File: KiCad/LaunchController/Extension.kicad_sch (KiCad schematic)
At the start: 3 parts, among them J17 CONN_STATUS_PANEL, J22 CONN_PANEL_BAORD_2, J23 CONN_PANEL_BAORD_1

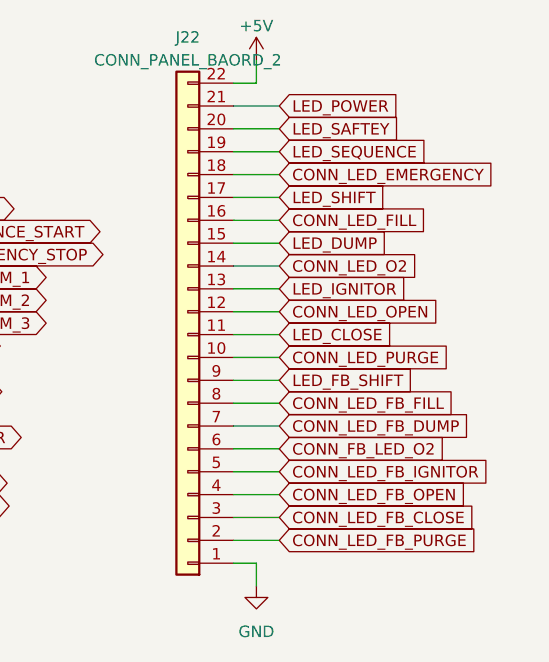
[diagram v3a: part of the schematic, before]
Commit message: シュミットトリガー無しで部品を配置
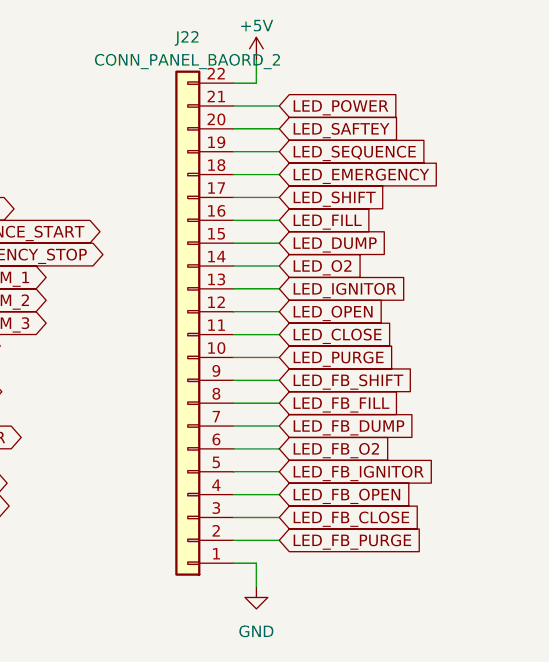
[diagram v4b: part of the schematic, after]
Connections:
- net CONN_FB_LED_O2 renamed LED_FB_O2
- net CONN_LED_EMERGENCY renamed LED_EMERGENCY
- net CONN_LED_FB_CLOSE renamed LED_FB_CLOSE
- net CONN_LED_FB_DUMP renamed LED_FB_DUMP
- net CONN_LED_FB_FILL renamed LED_FB_FILL
- net CONN_LED_FB_IGNITOR renamed LED_FB_IGNITOR
- net CONN_LED_FB_OPEN renamed LED_FB_OPEN
- net CONN_LED_FB_PURGE renamed LED_FB_PURGE
- net CONN_LED_FILL renamed LED_FILL
- net CONN_LED_O2 renamed LED_O2
- net CONN_LED_OPEN renamed LED_OPEN
- net CONN_LED_PURGE renamed LED_PURGE
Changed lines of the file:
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@@
     (stroke (width 0) (type default))
   )
-  (global_label "CONN_LED_FB_CLOSE" (shape input) (at 130.81 81.28 0) (fields_autoplaced)
-    (effects (font (size 1.27 1.27)) (justify left))
-    (property "Intersheetrefs" "${INTERSHEET_REFS}" (at 153.6729 81.28 0)
+  (global_label "LED_FB_CLOSE" (shape input) (at 130.81 81.28 0) (fields_autoplaced)
+    (effects (font (size 1.27 1.27)) (justify left))
+    (property "Intersheetrefs" "${INTERSHEET_REFS}" (at 147.4438 81.28 0)
       (effects (font (size 1.27 1.27)) (justify left) hide)
     )
@@
     )
   )
-  (global_label "CONN_LED_O2" (shape input) (at 130.81 53.34 0) (fields_autoplaced)
-    (effects (font (size 1.27 1.27)) (justify left))
-    (property "Intersheetrefs" "${INTERSHEET_REFS}" (at 146.8996 53.34 0)
-      (effects (font (size 1.27 1.27)) (justify left) hide)
-    )
-  )
-  (global_label "CONN_LED_EMERGENCY" (shape input) (at 130.81 43.18 0) (fields_autoplaced)
-    (effects (font (size 1.27 1.27)) (justify left))
-    (property "Intersheetrefs" "${INTERSHEET_REFS}" (at 155.4871 43.18 0)
-      (effects (font (size 1.27 1.27)) (justify left) hide)
-    )
-  )
-  (global_label "CONN_LED_FB_IGNITOR" (shape input) (at 130.81 76.2 0) (fields_autoplaced)
-    (effects (font (size 1.27 1.27)) (justify left))
-    (property "Intersheetrefs" "${INTERSHEET_REFS}" (at 155.064 76.2 0)
+  (global_label "LED_O2" (shape input) (at 130.81 53.34 0) (fields_autoplaced)
+    (effects (font (size 1.27 1.27)) (justify left))
+    (property "Intersheetrefs" "${INTERSHEET_REFS}" (at 140.6705 53.34 0)
+      (effects (font (size 1.27 1.27)) (justify left) hide)
+    )
+  )
+  (global_label "LED_EMERGENCY" (shape input) (at 130.81 43.18 0) (fields_autoplaced)
+    (effects (font (size 1.27 1.27)) (justify left))
+    (property "Intersheetrefs" "${INTERSHEET_REFS}" (at 149.258 43.18 0)
+      (effects (font (size 1.27 1.27)) (justify left) hide)
+    )
+  )
+  (global_label "LED_FB_IGNITOR" (shape input) (at 130.81 76.2 0) (fields_autoplaced)
+    (effects (font (size 1.27 1.27)) (justify left))
+    (property "Intersheetrefs" "${INTERSHEET_REFS}" (at 148.8349 76.2 0)
       (effects (font (size 1.27 1.27)) (justify left) hide)
     )
@@
     )
   )
-  (global_label "CONN_LED_FB_OPEN" (shape input) (at 130.81 78.74 0) (fields_autoplaced)
-    (effects (font (size 1.27 1.27)) (justify left))
-    (property "Intersheetrefs" "${INTERSHEET_REFS}" (at 152.7658 78.74 0)
-      (effects (font (size 1.27 1.27)) (justify left) hide)
-    )
-  )
-  (global_label "CONN_LED_FB_FILL" (shape input) (at 130.81 68.58 0) (fields_autoplaced)
-    (effects (font (size 1.27 1.27)) (justify left))
-    (property "Intersheetrefs" "${INTERSHEET_REFS}" (at 151.4354 68.58 0)
-      (effects (font (size 1.27 1.27)) (justify left) hide)
-    )
-  )
-  (global_label "CONN_LED_FILL" (shape input) (at 130.81 48.26 0) (fields_autoplaced)
-    (effects (font (size 1.27 1.27)) (justify left))
-    (property "Intersheetrefs" "${INTERSHEET_REFS}" (at 148.1092 48.26 0)
+  (global_label "LED_FB_OPEN" (shape input) (at 130.81 78.74 0) (fields_autoplaced)
+    (effects (font (size 1.27 1.27)) (justify left))
+    (property "Intersheetrefs" "${INTERSHEET_REFS}" (at 146.5367 78.74 0)
+      (effects (font (size 1.27 1.27)) (justify left) hide)
+    )
+  )
+  (global_label "LED_FB_FILL" (shape input) (at 130.81 68.58 0) (fields_autoplaced)
+    (effects (font (size 1.27 1.27)) (justify left))
+    (property "Intersheetrefs" "${INTERSHEET_REFS}" (at 145.2063 68.58 0)
+      (effects (font (size 1.27 1.27)) (justify left) hide)
+    )
+  )
+  (global_label "LED_FILL" (shape input) (at 130.81 48.26 0) (fields_autoplaced)
+    (effects (font (size 1.27 1.27)) (justify left))
+    (property "Intersheetrefs" "${INTERSHEET_REFS}" (at 141.8801 48.26 0)
       (effects (font (size 1.27 1.27)) (justify left) hide)
     )
@@
     )
   )
-  (global_label "CONN_LED_FB_PURGE" (shape input) (at 130.81 83.82 0) (fields_autoplaced)
-    (effects (font (size 1.27 1.27)) (justify left))
-    (property "Intersheetrefs" "${INTERSHEET_REFS}" (at 153.9753 83.82 0)
+  (global_label "LED_FB_PURGE" (shape input) (at 130.81 83.82 0) (fields_autoplaced)
+    (effects (font (size 1.27 1.27)) (justify left))
+    (property "Intersheetrefs" "${INTERSHEET_REFS}" (at 147.7462 83.82 0)
       (effects (font (size 1.27 1.27)) (justify left) hide)
     )
@@
     )
   )
-  (global_label "CONN_LED_OPEN" (shape input) (at 130.81 58.42 0) (fields_autoplaced)
-    (effects (font (size 1.27 1.27)) (justify left))
-    (property "Intersheetrefs" "${INTERSHEET_REFS}" (at 149.4396 58.42 0)
-      (effects (font (size 1.27 1.27)) (justify left) hide)
-    )
-  )
-  (global_label "CONN_LED_FB_DUMP" (shape input) (at 130.81 71.12 0) (fields_autoplaced)
-    (effects (font (size 1.27 1.27)) (justify left))
-    (property "Intersheetrefs" "${INTERSHEET_REFS}" (at 153.0077 71.12 0)
-      (effects (font (size 1.27 1.27)) (justify left) hide)
-    )
-  )
-  (global_label "CONN_FB_LED_O2" (shape input) (at 130.81 73.66 0) (fields_autoplaced)
-    (effects (font (size 1.27 1.27)) (justify left))
-    (property "Intersheetrefs" "${INTERSHEET_REFS}" (at 150.2258 73.66 0)
+  (global_label "LED_OPEN" (shape input) (at 130.81 58.42 0) (fields_autoplaced)
+    (effects (font (size 1.27 1.27)) (justify left))
+    (property "Intersheetrefs" "${INTERSHEET_REFS}" (at 143.2105 58.42 0)
+      (effects (font (size 1.27 1.27)) (justify left) hide)
+    )
+  )
+  (global_label "LED_FB_DUMP" (shape input) (at 130.81 71.12 0) (fields_autoplaced)
+    (effects (font (size 1.27 1.27)) (justify left))
+    (property "Intersheetrefs" "${INTERSHEET_REFS}" (at 146.7786 71.12 0)
+      (effects (font (size 1.27 1.27)) (justify left) hide)
+    )
+  )
+  (global_label "LED_FB_O2" (shape input) (at 130.81 73.66 0) (fields_autoplaced)
+    (effects (font (size 1.27 1.27)) (justify left))
+    (property "Intersheetrefs" "${INTERSHEET_REFS}" (at 143.9967 73.66 0)
       (effects (font (size 1.27 1.27)) (justify left) hide)
     )
@@
     )
   )
-  (global_label "CONN_LED_PURGE" (shape input) (at 130.81 63.5 0) (fields_autoplaced)
-    (effects (font (size 1.27 1.27)) (justify left))
-    (property "Intersheetrefs" "${INTERSHEET_REFS}" (at 150.6491 63.5 0)
-      (effects (font (size 1.27 1.27)) (justify left) hide)
-    )
+  (global_label "LED_PURGE" (shape input) (at 130.81 63.5 0) (fields_autoplaced)
+    (effects (font (size 1.27 1.27)) (justify left))
+    (property "Intersheetrefs" "${INTERSHEET_REFS}" (at 144.42 63.5 0)
+      (effects (font (size 1.27 1.27)) (justify left) hide)
+    )

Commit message: リセット
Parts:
- renumbered J17 to J7, J22 to J8, J23 to J9
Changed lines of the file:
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@@
   (symbol (lib_id "Connector_Generic:Conn_01x22") (at 120.65 60.96 180) (unit 1)
     (in_bom yes) (on_board yes) (dnp no) (fields_autoplaced)
-    (property "Reference" "J22" (at 120.65 27.94 0)
+    (property "Reference" "J8" (at 120.65 27.94 0)
       (effects (font (size 1.27 1.27)))
     )
@@
       (project "LaunchController"
         (path "/628d040b-43bf-4733-804f-091644a90124/7294b7f8-79a7-4ea3-8687-92a673d94882"
-          (reference "J22") (unit 1)
+          (reference "J8") (unit 1)
         )
       )
@@
   (symbol (lib_id "Connector_Generic:Conn_01x18") (at 78.74 62.23 180) (unit 1)
     (in_bom yes) (on_board yes) (dnp no) (fields_autoplaced)
-    (property "Reference" "J23" (at 78.74 34.29 0)
+    (property "Reference" "J9" (at 78.74 34.29 0)
       (effects (font (size 1.27 1.27)))
     )
@@
       (project "LaunchController"
         (path "/628d040b-43bf-4733-804f-091644a90124/7294b7f8-79a7-4ea3-8687-92a673d94882"
-          (reference "J23") (unit 1)
+          (reference "J9") (unit 1)
         )
       )
@@
         )
         (path "/628d040b-43bf-4733-804f-091644a90124/7294b7f8-79a7-4ea3-8687-92a673d94882"
-          (reference "#PWR080") (unit 1)
+          (reference "#PWR049") (unit 1)
         )
       )
@@
         )
         (path "/628d040b-43bf-4733-804f-091644a90124/7294b7f8-79a7-4ea3-8687-92a673d94882"
-          (reference "#PWR083") (unit 1)
+          (reference "#PWR048") (unit 1)
         )
       )
@@
   (symbol (lib_id "Connector_Generic:Conn_01x14") (at 27.94 60.96 180) (unit 1)
     (in_bom yes) (on_board yes) (dnp no) (fields_autoplaced)
-    (property "Reference" "J17" (at 27.94 38.1 0)
+    (property "Reference" "J7" (at 27.94 38.1 0)
       (effects (font (size 1.27 1.27)))
     )
@@
       (project "LaunchController"
         (path "/628d040b-43bf-4733-804f-091644a90124/7294b7f8-79a7-4ea3-8687-92a673d94882"
-          (reference "J17") (unit 1)
+          (reference "J7") (unit 1)
         )
       )
@@
   (symbol (lib_id "power:GND") (at 35.56 78.74 0) (unit 1)
     (in_bom yes) (on_board yes) (dnp no) (fields_autoplaced)
-    (property "Reference" "#PWR067" (at 35.56 85.09 0)
+    (property "Reference" "#PWR051" (at 35.56 85.09 0)
       (effects (font (size 1.27 1.27)) hide)
     )
@@
       (project "LaunchController"
         (path "/628d040b-43bf-4733-804f-091644a90124/7294b7f8-79a7-4ea3-8687-92a673d94882"
-          (reference "#PWR067") (unit 1)
+          (reference "#PWR051") (unit 1)
         )
       )
@@
   (symbol (lib_id "power:GND") (at 86.36 85.09 0) (unit 1)
     (in_bom yes) (on_board yes) (dnp no) (fields_autoplaced)
-    (property "Reference" "#PWR082" (at 86.36 91.44 0)
+    (property "Reference" "#PWR052" (at 86.36 91.44 0)
       (effects (font (size 1.27 1.27)) hide)
     )
@@
       (project "LaunchController"
         (path "/628d040b-43bf-4733-804f-091644a90124/7294b7f8-79a7-4ea3-8687-92a673d94882"
-          (reference "#PWR082") (unit 1)
+          (reference "#PWR052") (unit 1)
         )
       )
@@
         )
         (path "/628d040b-43bf-4733-804f-091644a90124/7294b7f8-79a7-4ea3-8687-92a673d94882"
-          (reference "#PWR079") (unit 1)
+          (reference "#PWR050") (unit 1)
         )
       )
@@
   (symbol (lib_id "power:GND") (at 128.27 88.9 0) (unit 1)
     (in_bom yes) (on_board yes) (dnp no) (fields_autoplaced)
-    (property "Reference" "#PWR081" (at 128.27 95.25 0)
+    (property "Reference" "#PWR053" (at 128.27 95.25 0)
       (effects (font (size 1.27 1.27)) hide)
     )
@@
       (project "LaunchController"
         (path "/628d040b-43bf-4733-804f-091644a90124/7294b7f8-79a7-4ea3-8687-92a673d94882"
-          (reference "#PWR081") (unit 1)
-        )
-      )
+          (reference "#PWR053") (unit 1)
+        )
+      )

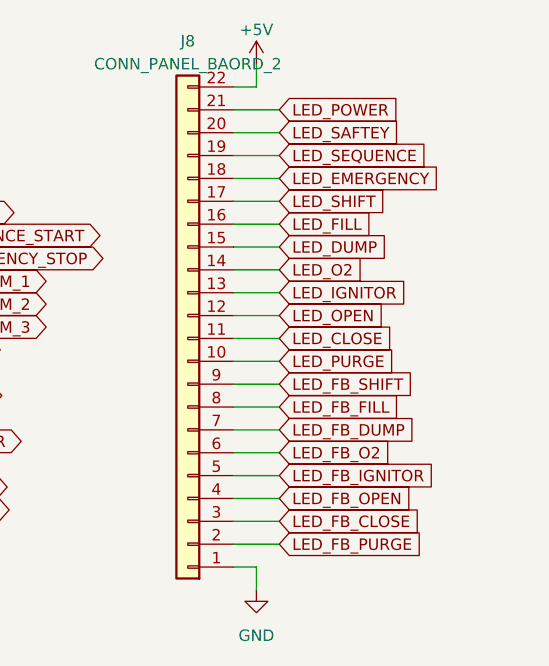
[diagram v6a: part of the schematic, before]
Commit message: ジャンパーを回路図に追加
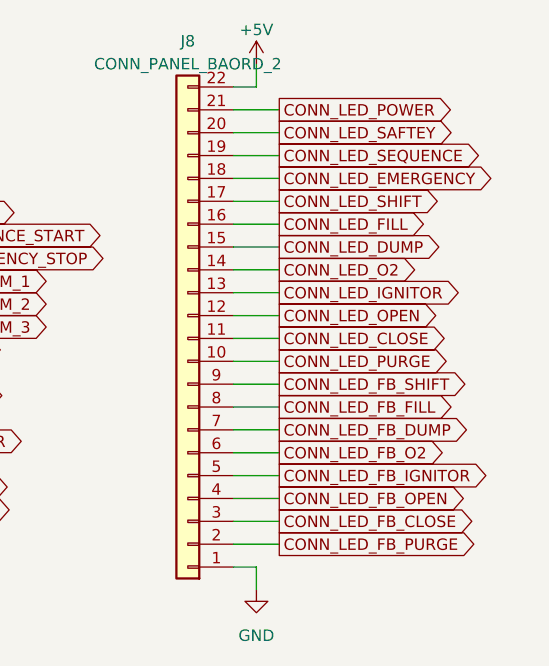
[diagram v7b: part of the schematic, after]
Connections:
- net LED_CLOSE renamed CONN_LED_CLOSE
- net LED_DUMP renamed CONN_LED_DUMP
- net LED_EMERGENCY renamed CONN_LED_EMERGENCY
- net LED_FB_CLOSE renamed CONN_LED_FB_CLOSE
- net LED_FB_DUMP renamed CONN_LED_FB_DUMP
- net LED_FB_FILL renamed CONN_LED_FB_FILL
- net LED_FB_IGNITOR renamed CONN_LED_FB_IGNITOR
- net LED_FB_O2 renamed CONN_LED_FB_O2
- net LED_FB_OPEN renamed CONN_LED_FB_OPEN
- net LED_FB_PURGE renamed CONN_LED_FB_PURGE
- net LED_FB_SHIFT renamed CONN_LED_FB_SHIFT
- net LED_FILL renamed CONN_LED_FILL
- net LED_IGNITOR renamed CONN_LED_IGNITOR
- net LED_O2 renamed CONN_LED_O2
- net LED_OPEN renamed CONN_LED_OPEN
- net LED_POWER renamed CONN_LED_POWER
- net LED_PURGE renamed CONN_LED_PURGE
- net LED_SAFTEY renamed CONN_LED_SAFTEY
- net LED_SEQUENCE renamed CONN_LED_SEQUENCE
- net LED_SHIFT renamed CONN_LED_SHIFT

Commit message: ランコンおわり
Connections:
- net CONN_LED_CLOSE: now also J8.16 (Pin_16); no longer J8.11 (Pin_11)
- net CONN_LED_EMERGENCY: now also J8.21 (Pin_21); no longer J8.18 (Pin_18)
- net CONN_LED_FB_CLOSE: now also J8.8 (Pin_8); no longer J8.3 (Pin_3)
- net CONN_LED_FB_FILL: now also J8.5 (Pin_5); no longer J8.8 (Pin_8)
- net CONN_LED_FB_IGNITOR: now also J8.4 (Pin_4); no longer J8.5 (Pin_5)
- net CONN_LED_FB_O2: now also J8.9 (Pin_9); no longer J8.6 (Pin_6)
- net CONN_LED_FB_OPEN: now also J8.6 (Pin_6); no longer J8.4 (Pin_4)
- net CONN_LED_FB_PURGE: now also J8.10 (Pin_10); no longer J8.2 (Pin_2)
- net CONN_LED_FB_SHIFT: now also J8.3 (Pin_3); no longer J8.9 (Pin_9)
- net CONN_LED_FILL: now also J8.13 (Pin_13); no longer J8.16 (Pin_16)
- net CONN_LED_IGNITOR: now also J8.12 (Pin_12); no longer J8.13 (Pin_13)
- net CONN_LED_O2: now also J8.17 (Pin_17); no longer J8.14 (Pin_14)
- net CONN_LED_OPEN: now also J8.14 (Pin_14); no longer J8.12 (Pin_12)
- net CONN_LED_POWER: now also J8.2 (Pin_2); no longer J8.21 (Pin_21)
- net CONN_LED_PURGE: now also J8.18 (Pin_18); no longer J8.10 (Pin_10)
- net CONN_LED_SHIFT: now also J8.11 (Pin_11); no longer J8.17 (Pin_17)
- net SW_CLOSE: now also J9.11 (Pin_11); no longer J9.3 (Pin_3)
- net SW_CONFIRM_2: now also J9.14 (Pin_14); no longer J9.11 (Pin_11)
- net SW_CONFIRM_3: now also J9.16 (Pin_16); no longer J9.10 (Pin_10)
- net SW_DUMP: now also J9.13 (Pin_13); no longer J9.7 (Pin_7)
- net SW_EMERGENCY_STOP: now also J9.3 (Pin_3); no longer J9.13 (Pin_13)
- net SW_FILL: now also J9.9 (Pin_9); no longer J9.8 (Pin_8)
- net SW_KILL: now also J9.8 (Pin_8); no longer J9.16 (Pin_16)
- net SW_O2: now also J9.17 (Pin_17); no longer J9.6 (Pin_6)
- net SW_OPEN: now also J9.7 (Pin_7); no longer J9.4 (Pin_4)
- net SW_PURGE: now also J9.15 (Pin_15); no longer J9.2 (Pin_2)
- net SW_RUN: now also J9.10 (Pin_10); no longer J9.17 (Pin_17)
- net SW_SAFETY: now also J9.2 (Pin_2); no longer J9.15 (Pin_15)
- net SW_SEQUENCE_START: now also J9.4 (Pin_4); no longer J9.14 (Pin_14)
- net SW_SHIFT: now also J9.6 (Pin_6); no longer J9.9 (Pin_9)
